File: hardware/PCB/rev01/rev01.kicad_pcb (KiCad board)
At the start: 2 copper layers, 100 x 50 mm, 81 parts, among them J2 CONSMA006.062, J4 USB_C_Receptacle_USB2.0_16P, J5 GPS_ANT, Q4 DMG3415U, SW1 RESET, SW2 BOOT, U1 NEO-M8N, U10 AP7313-15SAG-7, U2 ESP32-S3-WROOM-1, U3 SGTL5000XNLA3, U4 MAX17048G+T10, U5 SA818S, U6 MCP73831T-2ACI/OT, U7 AP2112K-3.3, U8 USBLC6-2P6, U9 0500LP15A500E

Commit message: progress on pcb
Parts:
- added S1: JS102011SAQN, PAKT_Local_Fp:SW_JS102011SAQN, F.Cu at (51.9, 62.6)
- added SW3: RIGHT, Button_Switch_SMD:SW_SPST_TL3342, F.Cu at (94.2, 95.7)
- added SW4: OK, Button_Switch_SMD:SW_SPST_TL3342, F.Cu at (94.2, 82.3)
- added SW5: Left, Button_Switch_SMD:SW_SPST_TL3342, F.Cu at (94.2, 89.4)
- C11, C12, C13, C15, C16, C3, C4, C5, C6, FB2, U10, U3: moved to B.Cu
- moved R3 65.0 mm to (101.1, 72.4)
- moved R4 65.0 mm to (102.9, 72.4)
- moved C17 42.6 mm to (99.4, 77.6), turned to 180 degrees
- moved J4 42.1 mm to (64.7, 53.7), turned to 0 degrees
- moved C27 41.4 mm to (101.7, 57.3), turned to 90 degrees
- moved R14 39.9 mm to (68.1, 74.0)
- moved SW2 39.9 mm to (70.8, 70.1)
- moved C28 39.2 mm to (99.5, 57.4), turned to 90 degrees
- moved J5 37.6 mm to (85.4, 96.4), turned to 0 degrees
- moved C26 37.5 mm to (82.6, 97.6), turned to 90 degrees
- moved C21 36.9 mm to (103.1, 61.4), turned to -90 degrees
- moved C6 36.8 mm to (115.9, 59.1), turned to 90 degrees
- moved C12 36.8 mm to (117.6, 59.1), turned to 90 degrees
- moved C3 36.7 mm to (119.8, 59.2), turned to 90 degrees
- moved C13 36.7 mm to (121.5, 59.2), turned to 90 degrees
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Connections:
- Q4 pad D: VBAT -> VBAT_SWITCHED
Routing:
- net VBAT: track 0.00 -> 46.2 mm
- net +5V_SA818: track 0.00 -> 40.7 mm
- net GND USB OUT: track 0.00 -> 21.2 mm
- net Net-(D15-K): track 0.00 -> 17.8 mm
- net ESP_EN: track 0.00 -> 15.5 mm
- net GND: track 0.00 -> 14.5 mm
- net VBUS: track 0.00 -> 14.2 mm
- net VDDIO: track 0.00 -> 13.5 mm
- net Net-(D6-K): track 0.00 -> 13.3 mm
- net USB_IN_POWER: track 0.00 -> 9.26 mm
- net ESP_IO0: track 0.00 -> 7.97 mm
- net VBCKP: track 0.00 -> 5.47 mm
- net Net-(D5-K): track 0.00 -> 4.73 mm
- net DD-: track 0.00 -> 4.73 mm
- net +3.3V-GPS: track 0.00 -> 4.38 mm
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
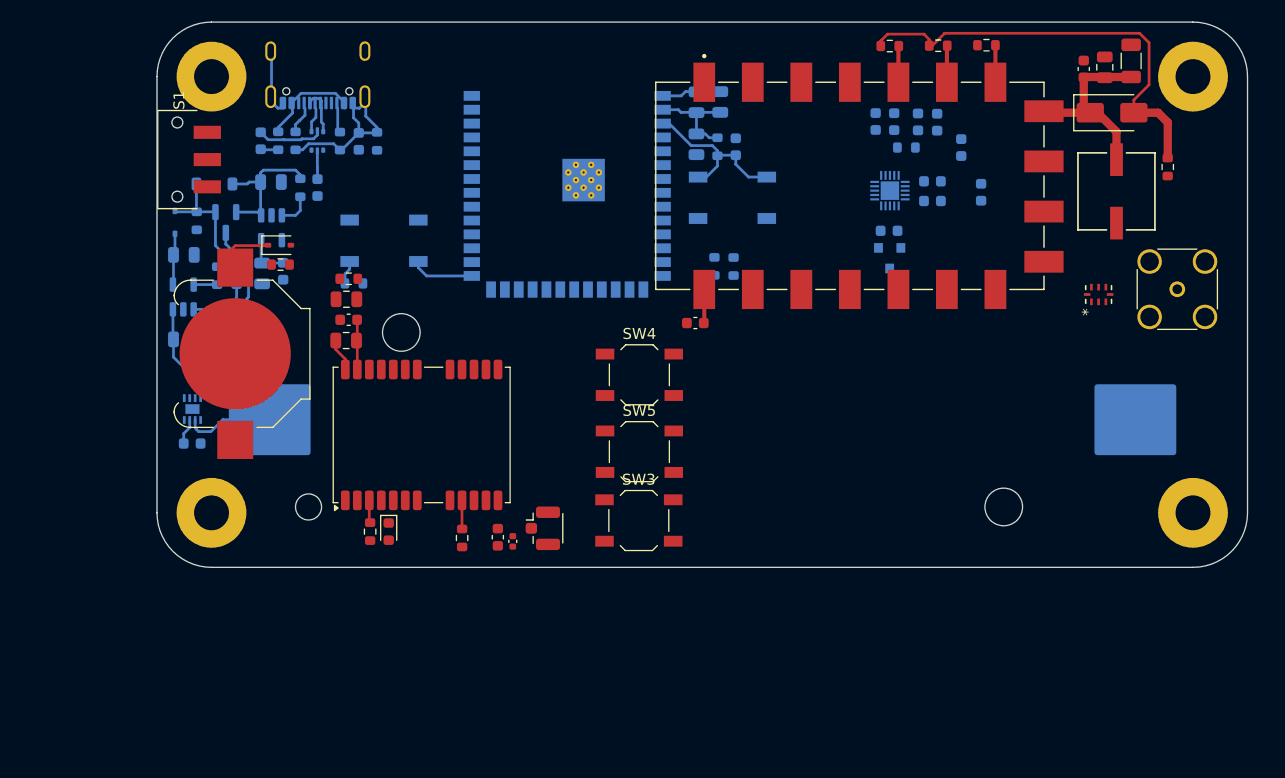
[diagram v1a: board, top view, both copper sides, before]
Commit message: added e-paper display
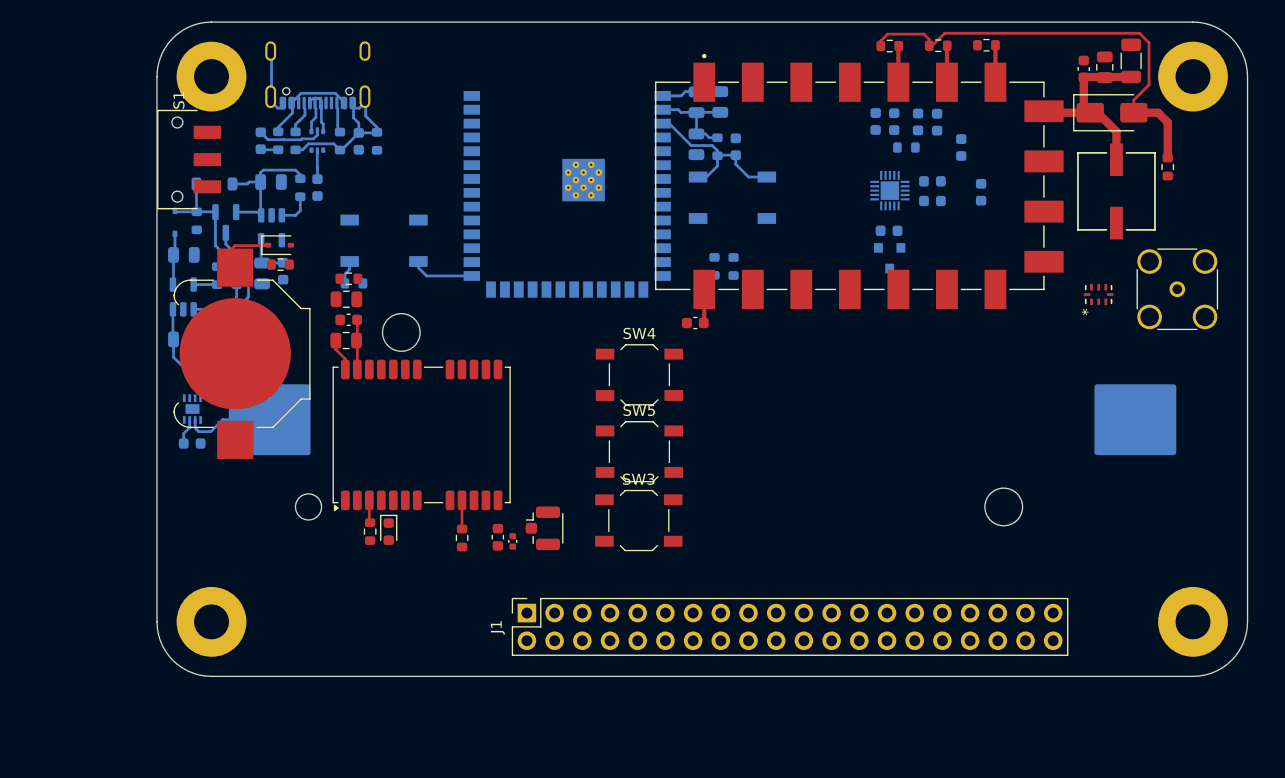
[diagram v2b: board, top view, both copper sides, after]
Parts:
- added J1: EPAPER_HAT_40PIN, Connector_PinSocket_2.54mm:PinSocket_2x20_P2.54mm_Vertical, F.Cu at (83.9, 104.2)
- moved H2 10.00 mm to (145.0, 105.0)
- moved H4 10.00 mm to (55.0, 105.0)
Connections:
- U2 pad 23: unconnected-(U2-IO21-Pad23) -> EPD_DIN
- U2 pad 31: unconnected-(U2-IO38-Pad31) -> EPD_BUSY
- U2 pad 32: unconnected-(U2-IO39-Pad32) -> EPD_PWR_EN
- U2 pad 5: unconnected-(U2-IO5-Pad5) -> EPD_CS
- U2 pad 6: unconnected-(U2-IO6-Pad6) -> EPD_DC
- U2 pad 7: unconnected-(U2-IO7-Pad7) -> EPD_RST
- U2 pad 9: unconnected-(U2-IO16-Pad9) -> EPD_SCLK
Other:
- board size 100 x 50 mm -> 100 x 60 mm
